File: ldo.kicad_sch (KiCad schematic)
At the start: 0 parts

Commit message: Update ldo.kicad_sch
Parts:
- added C1, C2: 0805Capacitor, CAPC2012X94N, symbol group127:0805Capacitor
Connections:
- new net 5V: C1.2, C2.1, C2.2
- new net Output: C1.1

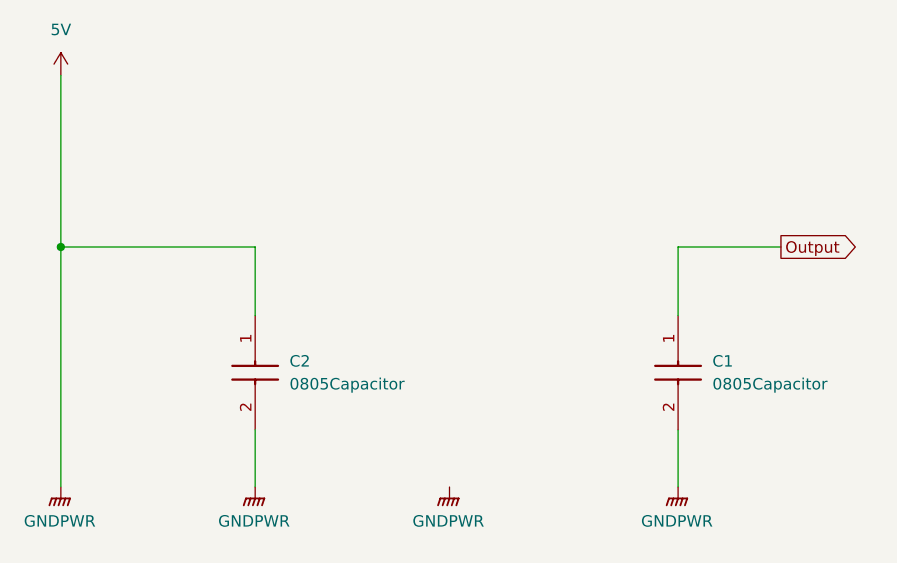
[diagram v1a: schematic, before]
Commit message: LDO changes from camryn
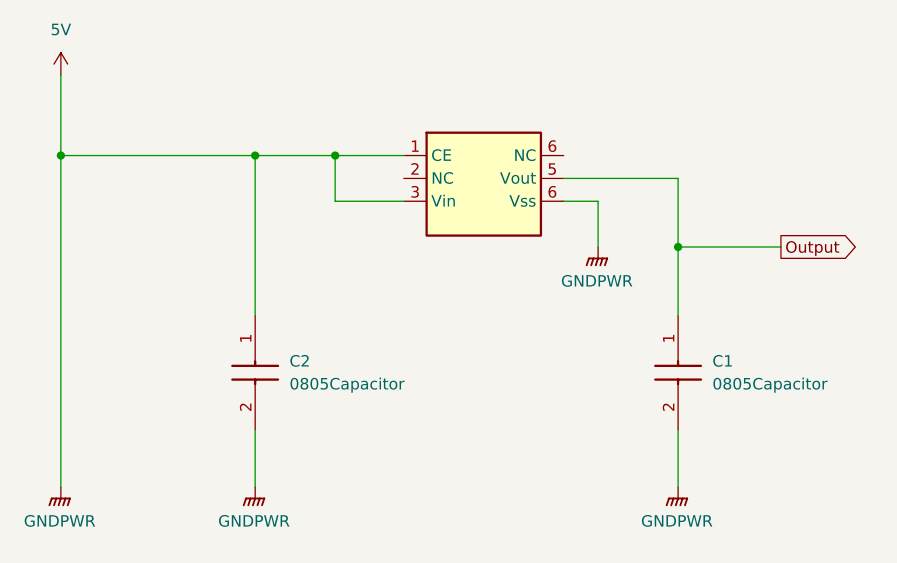
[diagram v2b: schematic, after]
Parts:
- added X?: ~, XC6210A332MR-G1, symbol group127:XC6210A332MR-G
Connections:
- net 5V: now also X?.1 (CE), X?.3 (Vin), X?.6 (Vss)
- net Output: now also X?.5 (Vout)
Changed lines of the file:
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@@
 	(paper "A4")
 	(junction
-		(at 119.38 90.17)
+		(at 140.97 80.01)
 		(diameter 0)
 		(color 0 0 0 0)
 	)
-	(wire
-		(pts
-			(xy 119.38 90.17) (xy 140.97 90.17)
+	(junction
+		(at 149.86 80.01)
+		(diameter 0)
+		(color 0 0 0 0)
+	)
+	(junction
+		(at 119.38 80.01)
+		(diameter 0)
+		(color 0 0 0 0)
+	)
+	(junction
+		(at 187.96 90.17)
+		(diameter 0)
+		(color 0 0 0 0)
+	)
+	(wire
+		(pts
+			(xy 187.96 82.55) (xy 187.96 90.17)
+		)
+		(stroke
+			(width 0)
+			(type default)
+		)
+	)
+	(wire
+		(pts
+			(xy 119.38 80.01) (xy 140.97 80.01)
 		)
 		(stroke
@@
 	(wire
 		(pts
+			(xy 140.97 80.01) (xy 149.86 80.01)
+		)
+		(stroke
+			(width 0)
+			(type default)
+		)
+	)
+	(wire
+		(pts
+			(xy 119.38 80.01) (xy 119.38 116.84)
+		)
+		(stroke
+			(width 0)
+			(type default)
+		)
+	)
+	(wire
+		(pts
 			(xy 187.96 90.17) (xy 199.39 90.17)
 		)
@@
 	(wire
 		(pts
-			(xy 119.38 71.12) (xy 119.38 90.17)
-		)
-		(stroke
-			(width 0)
-			(type default)
-		)
-	)
-	(wire
-		(pts
-			(xy 140.97 90.17) (xy 140.97 97.79)
+			(xy 119.38 71.12) (xy 119.38 80.01)
+		)
+		(stroke
+			(width 0)
+			(type default)
+		)
+	)
+	(wire
+		(pts
+			(xy 175.26 82.55) (xy 187.96 82.55)
+		)
+		(stroke
+			(width 0)
+			(type default)
+		)
+	)
+	(wire
+		(pts
+			(xy 157.48 85.09) (xy 149.86 85.09)
+		)
+		(stroke
+			(width 0)
+			(type default)
+		)
+	)
+	(wire
+		(pts
+			(xy 140.97 80.01) (xy 140.97 97.79)
 		)
 		(stroke
@@
 	(wire
 		(pts
-			(xy 119.38 90.17) (xy 119.38 116.84)
+			(xy 179.07 85.09) (xy 175.26 85.09)
+		)
+		(stroke
+			(width 0)
+			(type default)
+		)
+	)
+	(wire
+		(pts
+			(xy 149.86 85.09) (xy 149.86 80.01)
+		)
+		(stroke
+			(width 0)
+			(type default)
+		)
+	)
+	(wire
+		(pts
+			(xy 149.86 80.01) (xy 157.48 80.01)
+		)
+		(stroke
+			(width 0)
+			(type default)
+		)
+	)
+	(wire
+		(pts
+			(xy 179.07 90.17) (xy 179.07 85.09)
 		)
 		(stroke
@@
 	)
 	(symbol
+		(lib_id "group127:XC6210A332MR-G")
+		(at 166.37 82.55 0)
+		(unit 1)
+		(exclude_from_sim no)
+		(in_bom yes)
+		(on_board yes)
+		(dnp no)
+		(fields_autoplaced yes)
+		(property "Reference" "X?"
+			(at 166.116 75.184 0)
+			(effects
+				(font
+					(size 1.27 1.27)
+				)
+				(hide yes)
+			)
+		)
+		(property "Value" "~"
+			(at 172.72 76.2 0)
+			(effects
+				(font
+					(size 1.27 1.27)
+				)
+				(hide yes)
+			)
+		)
+		(property "Footprint" "XC6210A332MR-G1"
+			(at 167.132 68.834 0)
+			(effects
+				(font
+					(size 1.27 1.27)
+				)
+				(hide yes)
+			)
+		)
+		(property "Datasheet" "https://www.mouser.com/datasheet/2/760/xc6210-3371396.pdf"
+			(at 165.1 63.5 0)
+			(effects
+				(font
+					(size 1.27 1.27)
+				)
+				(hide yes)
+			)
+		)
+		(property "Description" "LDO Voltage Regulators 700mA High Speed LDO Regulator"
+			(at 165.608 102.87 0)
+			(effects
+				(font
+					(size 1.27 1.27)
+				)
+				(hide yes)
+			)
+		)
+		(pin "6"
+		)
+		(pin "6"
+		)
+		(pin "2"
+		)
+		(pin "5"
+		)
+		(pin "1"
+		)
+		(pin "3"
+		)
+		(instances
+			(project ""
+				(path "/5ce3566e-4e0f-420e-9b0d-3952cd3c63fd/06c65770-b1a9-4683-9717-b848c80eccc4"
+					(reference "X?")
+					(unit 1)
+				)
+			)
+		)
+	)
+	(symbol
 		(lib_id "power:GNDPWR")
 		(at 187.96 116.84 0)
@@
 	(symbol
 		(lib_id "power:GNDPWR")
-		(at 162.56 116.84 0)
+		(at 179.07 90.17 0)
 		(unit 1)
 		(exclude_from_sim no)
@@
 		(fields_autoplaced yes)
 		(property "Reference" "#PWR03"
-			(at 162.56 121.92 0)
+			(at 179.07 95.25 0)
 			(effects
 				(font
@@
 		)
 		(property "Value" "GNDPWR"
-			(at 162.433 120.65 0)
+			(at 178.943 93.98 0)
 			(effects
 				(font
@@
 		)
 		(property "Footprint" ""
-			(at 162.56 118.11 0)
+			(at 179.07 91.44 0)
 			(effects
 				(font
@@
 		)
 		(property "Datasheet" ""
-			(at 162.56 118.11 0)
+			(at 179.07 91.44 0)
 			(effects
 				(font
@@
 		)
 		(property "Description" "Power symbol creates a global label with name \"GNDPWR\" , global ground"
-			(at 162.56 116.84 0)
-			(effects
-				(font
+			(at 179.07 90.17 0)
+			(effects
+				(font

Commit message: New gnd symbol
Changed ground symbol in LDO
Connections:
- net 5V: no longer C1.2, C2.2, X?.6 (Vss)
- net GND: now reaches X?.6 (Vss)
- net GND: now also C1.2, C2.2
- no-connect marks 0 -> 2

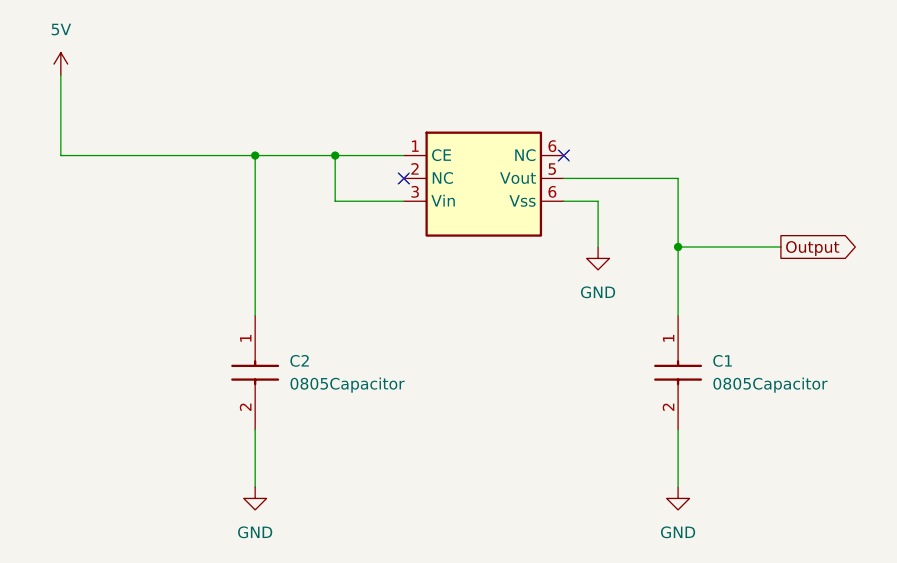
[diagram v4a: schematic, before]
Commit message: standardize 5V and 3V3 labels
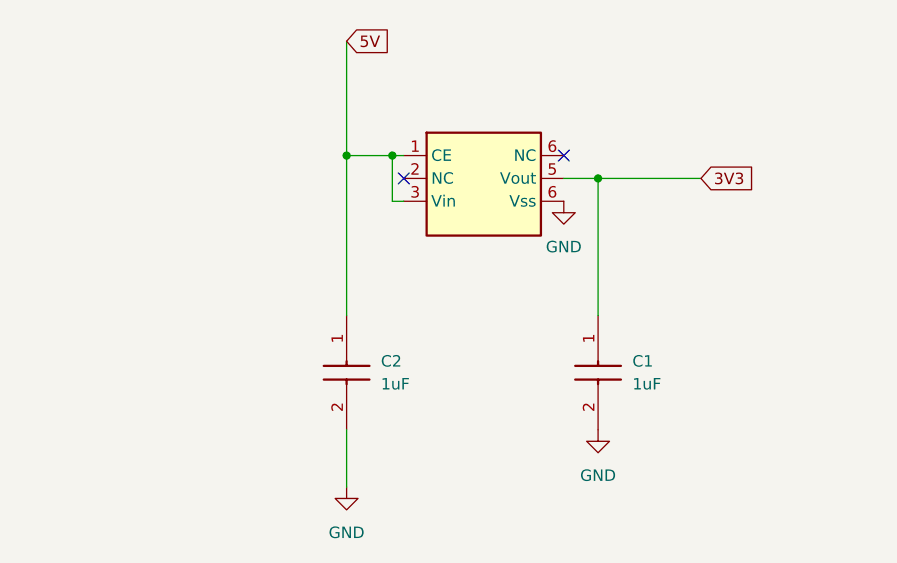
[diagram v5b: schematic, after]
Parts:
- C1, C2: value 0805Capacitor -> 1uF
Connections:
- net Output renamed 3V3
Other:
- moved on the sheet: C1, C2

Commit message: finished up schematic
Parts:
- C6: renamed from C2; footprint CAPC2012X94N -> Capacitor_SMD:C_0805_2012Metric
- C7: renamed from C1; footprint CAPC2012X94N -> Capacitor_SMD:C_0805_2012Metric
- IC4: renamed from X?; value ~ -> LDO; footprint XC6210A332MR-G1 -> (none)
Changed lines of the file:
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@@
 		(dnp no)
 		(fields_autoplaced yes)
-		(property "Reference" "#PWR?"
+		(property "Reference" "#PWR020"
 			(at 179.07 116.84 0)
 			(effects
@@
 			(project "harm_drone"
 				(path "/5ce3566e-4e0f-420e-9b0d-3952cd3c63fd/06c65770-b1a9-4683-9717-b848c80eccc4"
-					(reference "#PWR?")
+					(reference "#PWR020")
 					(unit 1)
 				)
@@
 		(dnp no)
 		(fields_autoplaced yes)
-		(property "Reference" "C2"
+		(property "Reference" "C6"
 			(at 154.94 102.8699 90)
 			(effects
@@
 			)
 		)
-		(property "Footprint" "CAPC2012X94N"
+		(property "Footprint" "Capacitor_SMD:C_0805_2012Metric"
 			(at 54.94 106.68 0)
 			(effects
@@
 			(project "harm_drone"
 				(path "/5ce3566e-4e0f-420e-9b0d-3952cd3c63fd/06c65770-b1a9-4683-9717-b848c80eccc4"
-					(reference "C2")
+					(reference "C6")
 					(unit 1)
 				)
@@
 		(dnp no)
 		(fields_autoplaced yes)
-		(property "Reference" "C1"
+		(property "Reference" "C7"
 			(at 182.88 102.8699 90)
 			(effects
@@
 			)
 		)
-		(property "Footprint" "CAPC2012X94N"
+		(property "Footprint" "Capacitor_SMD:C_0805_2012Metric"
 			(at 82.88 106.68 0)
 			(effects
@@
 			(project ""
 				(path "/5ce3566e-4e0f-420e-9b0d-3952cd3c63fd/06c65770-b1a9-4683-9717-b848c80eccc4"
-					(reference "C1")
+					(reference "C7")
 					(unit 1)
 				)
@@
 		(dnp no)
 		(fields_autoplaced yes)
-		(property "Reference" "#PWR?"
+		(property "Reference" "#PWR018"
 			(at 151.13 123.19 0)
 			(effects
@@
 			(project "harm_drone"
 				(path "/5ce3566e-4e0f-420e-9b0d-3952cd3c63fd/06c65770-b1a9-4683-9717-b848c80eccc4"
-					(reference "#PWR?")
+					(reference "#PWR018")
 					(unit 1)
 				)
@@
 		(dnp no)
 		(fields_autoplaced yes)
-		(property "Reference" "X?"
+		(property "Reference" "IC4"
 			(at 166.116 75.184 0)
 			(effects
@@
 			)
 		)
-		(property "Value" "~"
+		(property "Value" "LDO"
 			(at 172.72 76.2 0)
 			(effects
@@
 			)
 		)
-		(property "Footprint" "XC6210A332MR-G1"
+		(property "Footprint" ""
 			(at 167.132 68.834 0)
 			(effects
@@
 			(project ""
 				(path "/5ce3566e-4e0f-420e-9b0d-3952cd3c63fd/06c65770-b1a9-4683-9717-b848c80eccc4"
-					(reference "X?")
+					(reference "IC4")
 					(unit 1)
 				)
@@
 		(dnp no)
 		(fields_autoplaced yes)
-		(property "Reference" "#PWR?"
+		(property "Reference" "#PWR019"
 			(at 175.26 91.44 0)
 			(effects
@@
 			(project "harm_drone"
 				(path "/5ce3566e-4e0f-420e-9b0d-3952cd3c63fd/06c65770-b1a9-4683-9717-b848c80eccc4"
-					(reference "#PWR?")
-					(unit 1)
-				)
+					(reference "#PWR019")
+					(unit 1)
+				)

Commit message: initial PCB draft!
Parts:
- IC4: footprint (none) -> group127:LDO; symbol group127:XC6210A332MR-G -> group127:LDO; Height (none) -> 1.3; Manufacturer_Name (none) -> Torex; Manufacturer_Part_Number (none) -> XC6210A332MR-G; Mouser Part Number (none) -> 865-XC6210A332MR-G; Mouser Price/Stock (none) -> https://www.mouser.co.uk/ProductDetail/Torex-Semiconductor/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
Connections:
- net GND: now also IC4.2 (VSS); no longer IC4.6 (Vss)
- no-connect marks 2 -> 0
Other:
- moved on the sheet: C7
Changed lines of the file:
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@@
 	)
 	(junction
-		(at 179.07 82.55)
+		(at 189.23 82.55)
 		(diameter 0)
 		(color 0 0 0 0)
@@
 		(color 0 0 0 0)
 	)
-	(no_connect
-		(at 157.48 82.55)
-	)
-	(no_connect
-		(at 175.26 80.01)
+	(wire
+		(pts
+			(xy 157.48 82.55) (xy 154.94 82.55)
+		)
+		(stroke
+			(width 0)
+			(type default)
+		)
 	)
 	(wire
@@
 	(wire
 		(pts
-			(xy 179.07 82.55) (xy 179.07 97.79)
-		)
-		(stroke
-			(width 0)
-			(type default)
-		)
-	)
-	(wire
-		(pts
-			(xy 179.07 82.55) (xy 190.5 82.55)
+			(xy 189.23 82.55) (xy 189.23 97.79)
+		)
+		(stroke
+			(width 0)
+			(type default)
+		)
+	)
+	(wire
+		(pts
+			(xy 189.23 82.55) (xy 200.66 82.55)
 		)
 		(stroke
@@
 	(wire
 		(pts
-			(xy 175.26 82.55) (xy 179.07 82.55)
+			(xy 185.42 82.55) (xy 189.23 82.55)
 		)
 		(stroke
@@
 		(pts
 			(xy 151.13 80.01) (xy 151.13 97.79)
+		)
+		(stroke
+			(width 0)
+			(type default)
+		)
+	)
+	(wire
+		(pts
+			(xy 154.94 82.55) (xy 154.94 90.17)
 		)
 		(stroke
@@
 	(global_label "3V3"
 		(shape input)
-		(at 190.5 82.55 0)
+		(at 200.66 82.55 0)
 		(fields_autoplaced yes)
 		(effects
@@
 		)
 		(property "Intersheetrefs" "${INTERSHEET_REFS}"
-			(at 196.9928 82.55 0)
+			(at 207.1528 82.55 0)
 			(effects
 				(font
@@
 	(symbol
 		(lib_id "power:GND")
-		(at 179.07 110.49 0)
+		(at 189.23 110.49 0)
 		(unit 1)
 		(exclude_from_sim no)
@@
 		(fields_autoplaced yes)
 		(property "Reference" "#PWR020"
-			(at 179.07 116.84 0)
+			(at 189.23 116.84 0)
 			(effects
 				(font
@@
 		)
 		(property "Value" "GND"
-			(at 179.07 115.57 0)
+			(at 189.23 115.57 0)
 			(effects
 				(font
@@
 		)
 		(property "Footprint" ""
-			(at 179.07 110.49 0)
+			(at 189.23 110.49 0)
 			(effects
 				(font
@@
 		)
 		(property "Datasheet" ""
-			(at 179.07 110.49 0)
+			(at 189.23 110.49 0)
 			(effects
 				(font
@@
 		)
 		(property "Description" "Power symbol creates a global label with name \"GND\" , ground"
-			(at 179.07 110.49 0)
+			(at 189.23 110.49 0)
 			(effects
 				(font
@@
 	(symbol
 		(lib_id "group127:0805Capacitor")
-		(at 179.07 97.79 270)
+		(at 189.23 97.79 270)
 		(unit 1)
 		(exclude_from_sim no)
@@
 		(fields_autoplaced yes)
 		(property "Reference" "C7"
-			(at 182.88 102.8699 90)
+			(at 193.04 102.8699 90)
 			(effects
 				(font
@@
 		)
 		(property "Value" "1uF"
-			(at 182.88 105.4099 90)
+			(at 193.04 105.4099 90)
 			(effects
 				(font
@@
 		)
 		(property "Footprint" "Capacitor_SMD:C_0805_2012Metric"
-			(at 82.88 106.68 0)
+			(at 93.04 106.68 0)
 			(effects
 				(font
@@
 		)
 		(property "Datasheet" "http://datasheets.avx.com/X7RDielectric.pdf"
-			(at -17.12 106.68 0)
+			(at -6.96 106.68 0)
 			(effects
 				(font
@@
 		)
 		(property "Description" "0805 X7R ceramic capacitor,100nF 50V AVX 0805 Standard 100nF Ceramic Multilayer Capacitor, 50 V dc, +125degC, X7R Dielectric,  /-10% SMD"
-			(at 179.07 97.79 0)
+			(at 189.23 97.79 0)
 			(effects
 				(font
@@
 		)
 		(property "Height" "0.94"
-			(at -217.12 106.68 0)
+			(at -206.96 106.68 0)
 			(effects
 				(font
@@
 		)
 		(property "Mouser Part Number" "581-08055C104K"
-			(at -317.12 106.68 0)
+			(at -306.96 106.68 0)
 			(effects
 				(font
@@
 		)
 		(property "Mouser Price/Stock" "https://www.mouser.co.uk/ProductDetail/KYOCERA-AVX/08055C104KAT2A?qs=2ujN4bDBNE9mJvapP%252BjopA%3D%3D"
-			(at -417.12 106.68 0)
+			(at -406.96 106.68 0)
 			(effects
 				(font
@@
 		)
 		(property "Manufacturer_Name" "Kyocera AVX"
-			(at -517.12 106.68 0)
+			(at -506.96 106.68 0)
 			(effects
 				(font
@@
 		)
 		(property "Manufacturer_Part_Number" "08055C104KAT2A"
-			(at -617.12 106.68 0)
+			(at -606.96 106.68 0)
 			(effects
 				(font
@@
 	)
 	(symbol
-		(lib_id "group127:XC6210A332MR-G")
-		(at 166.37 82.55 0)
+		(lib_id "group127:LDO")
+		(at 157.48 80.01 0)
 		(unit 1)
 		(exclude_from_sim no)
@@
 		(fields_autoplaced yes)
 		(property "Reference" "IC4"
-			(at 166.116 75.184 0)
+			(at 157.226 72.644 0)
 			(effects
 				(font
@@
 		)
 		(property "Value" "LDO"
-			(at 172.72 76.2 0)
-			(effects
-				(font
-					(size 1.27 1.27)
-				)
-				(hide yes)
-			)
-		)
-		(property "Footprint" ""
-			(at 167.132 68.834 0)
-			(effects
-				(font
-					(size 1.27 1.27)
-				)
-				(hide yes)
-			)
-		)
-		(property "Datasheet" "https://www.mouser.com/datasheet/2/760/xc6210-3371396.pdf"
-			(at 165.1 63.5 0)
-			(effects
-				(font
-					(size 1.27 1.27)
-				)
+			(at 163.83 73.66 0)
+			(effects
+				(font
+					(size 1.27 1.27)
+				)
+				(hide yes)
+			)
+		)
+		(property "Footprint" "group127:LDO"
+			(at 181.61 174.93 0)
+			(effects
+				(font
+					(size 1.27 1.27)
+				)
+				(justify left top)
+				(hide yes)
+			)
+		)
+		(property "Datasheet" "https://www.torexsemi.com/file/xc6210/XC6210.pdf"
+			(at 181.61 274.93 0)
+			(effects
+				(font
+					(size 1.27 1.27)
+				)
+				(justify left top)
 				(hide yes)
 			)
 		)
 		(property "Description" "LDO Voltage Regulators 700mA High Speed LDO Regulator"
-			(at 165.608 102.87 0)
-			(effects
-				(font
-					(size 1.27 1.27)
-				)
-				(hide yes)
-			)
-		)
-		(pin "6"
-		)
-		(pin "6"
+			(at 157.48 80.01 0)
+			(effects
+				(font
+					(size 1.27 1.27)
+				)
+				(hide yes)
+			)
+		)
+		(property "Height" "1.3"
+			(at 181.61 474.93 0)
+			(effects
+				(font
+					(size 1.27 1.27)
+				)
+				(justify left top)
+				(hide yes)
+			)
+		)
+		(property "Mouser Part Number" "865-XC6210A332MR-G"
+			(at 181.61 574.93 0)
+			(effects
+				(font
+					(size 1.27 1.27)
+				)
+				(justify left top)
+				(hide yes)
+			)
+		)
+		(property "Mouser Price/Stock" "https://www.mouser.co.uk/ProductDetail/Torex-Semiconductor/XC6210A332MR-G?qs=AsjdqWjXhJ%252BGZM2kyDkSFw%3D%3D"
+			(at 181.61 674.93 0)
+			(effects
+				(font
+					(size 1.27 1.27)
+				)
+				(justify left top)
+				(hide yes)
+			)
+		)
+		(property "Manufacturer_Name" "Torex"
+			(at 181.61 774.93 0)
+			(effects
+				(font
+					(size 1.27 1.27)
+				)
+				(justify left top)
+				(hide yes)
+			)
+		)
+		(property "Manufacturer_Part_Number" "XC6210A332MR-G"
+			(at 181.61 874.93 0)
+			(effects
+				(font
+					(size 1.27 1.27)
+				)
+				(justify left top)
+				(hide yes)
+			)
+		)
+		(pin "4"
 		)
 		(pin "2"
@@
 	(symbol
 		(lib_id "power:GND")
-		(at 175.26 85.09 0)
+		(at 154.94 90.17 0)
 		(unit 1)
 		(exclude_from_sim no)
@@
 		(dnp no)
 		(fields_autoplaced yes)
-		(property "Reference" "#PWR019"
-			(at 175.26 91.44 0)
+		(property "Reference" "#PWR034"
+			(at 154.94 96.52 0)
 			(effects
 				(font
@@
 		)
 		(property "Value" "GND"
-			(at 175.26 90.17 0)
+			(at 154.94 95.25 0)
 			(effects
 				(font
@@
 		)
 		(property "Footprint" ""
-			(at 175.26 85.09 0)
+			(at 154.94 90.17 0)
 			(effects
 				(font
@@
 		)
 		(property "Datasheet" ""
-			(at 175.26 85.09 0)
+			(at 154.94 90.17 0)
 			(effects
 				(font
@@
 		)
 		(property "Description" "Power symbol creates a global label with name \"GND\" , ground"
-			(at 175.26 85.09 0)
+			(at 154.94 90.17 0)
 			(effects
 				(font
@@
 			(project "harm_drone"
 				(path "/5ce3566e-4e0f-420e-9b0d-3952cd3c63fd/06c65770-b1a9-4683-9717-b848c80eccc4"
-					(reference "#PWR019")
-					(unit 1)
-				)
-			)
-			(project "ldo"
-				(path "/8c89e2c6-3a4c-42d5-9469-c7cf807a96d1"
-					(reference "#PWR03")
-					(unit 1)
-				)
+					(reference "#PWR034")
+					(unit 1)
+				)

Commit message: final changes
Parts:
- renumbered C6 to C18, C7 to C19, IC4 to IC3
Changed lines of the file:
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@@
 		(dnp no)
 		(fields_autoplaced yes)
-		(property "Reference" "#PWR020"
+		(property "Reference" "#PWR022"
 			(at 189.23 116.84 0)
 			(effects
@@
 			(project "harm_drone"
 				(path "/5ce3566e-4e0f-420e-9b0d-3952cd3c63fd/06c65770-b1a9-4683-9717-b848c80eccc4"
-					(reference "#PWR020")
+					(reference "#PWR022")
 					(unit 1)
 				)
@@
 		(dnp no)
 		(fields_autoplaced yes)
-		(property "Reference" "C6"
+		(property "Reference" "C18"
 			(at 154.94 102.8699 90)
 			(effects
@@
 			(project "harm_drone"
 				(path "/5ce3566e-4e0f-420e-9b0d-3952cd3c63fd/06c65770-b1a9-4683-9717-b848c80eccc4"
-					(reference "C6")
+					(reference "C18")
 					(unit 1)
 				)
@@
 		(dnp no)
 		(fields_autoplaced yes)
-		(property "Reference" "C7"
+		(property "Reference" "C19"
 			(at 193.04 102.8699 90)
 			(effects
@@
 			(project ""
 				(path "/5ce3566e-4e0f-420e-9b0d-3952cd3c63fd/06c65770-b1a9-4683-9717-b848c80eccc4"
-					(reference "C7")
+					(reference "C19")
 					(unit 1)
 				)
@@
 		(dnp no)
 		(fields_autoplaced yes)
-		(property "Reference" "#PWR018"
+		(property "Reference" "#PWR020"
 			(at 151.13 123.19 0)
 			(effects
@@
 			(project "harm_drone"
 				(path "/5ce3566e-4e0f-420e-9b0d-3952cd3c63fd/06c65770-b1a9-4683-9717-b848c80eccc4"
-					(reference "#PWR018")
+					(reference "#PWR020")
 					(unit 1)
 				)
@@
 		(dnp no)
 		(fields_autoplaced yes)
-		(property "Reference" "IC4"
+		(property "Reference" "IC3"
 			(at 157.226 72.644 0)
 			(effects
@@
 			(project ""
 				(path "/5ce3566e-4e0f-420e-9b0d-3952cd3c63fd/06c65770-b1a9-4683-9717-b848c80eccc4"
-					(reference "IC4")
+					(reference "IC3")
 					(unit 1)
 				)
@@
 		(dnp no)
 		(fields_autoplaced yes)
-		(property "Reference" "#PWR034"
+		(property "Reference" "#PWR021"
 			(at 154.94 96.52 0)
 			(effects
@@
 			(project "harm_drone"
 				(path "/5ce3566e-4e0f-420e-9b0d-3952cd3c63fd/06c65770-b1a9-4683-9717-b848c80eccc4"
-					(reference "#PWR034")
-					(unit 1)
-				)
+					(reference "#PWR021")
+					(unit 1)
+				)
